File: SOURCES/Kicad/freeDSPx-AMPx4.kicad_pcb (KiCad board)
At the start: 2 copper layers, 60 x 100 mm, 283 parts, among them P1 CONN_01X02, P2 STDCONN, P3 CONN_01X02, P4 CONN_01X02, P5 CONN_01X02, P6 CONN_01X02, U1 LM2841X, U2 TAS5720M, U3 TAS5720M, U4 TAS5720M, U5 TAS5720M

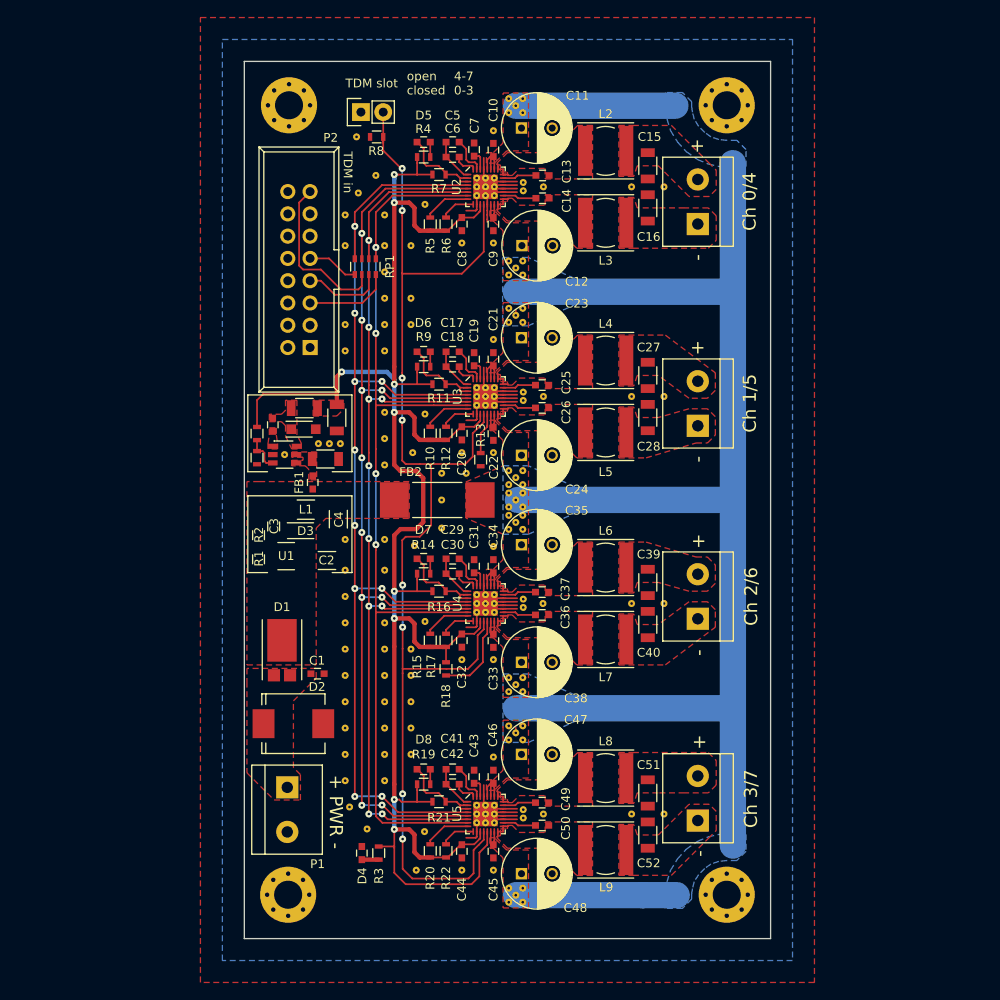
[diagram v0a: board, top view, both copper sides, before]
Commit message: Changed VQFN footprint to solderable.
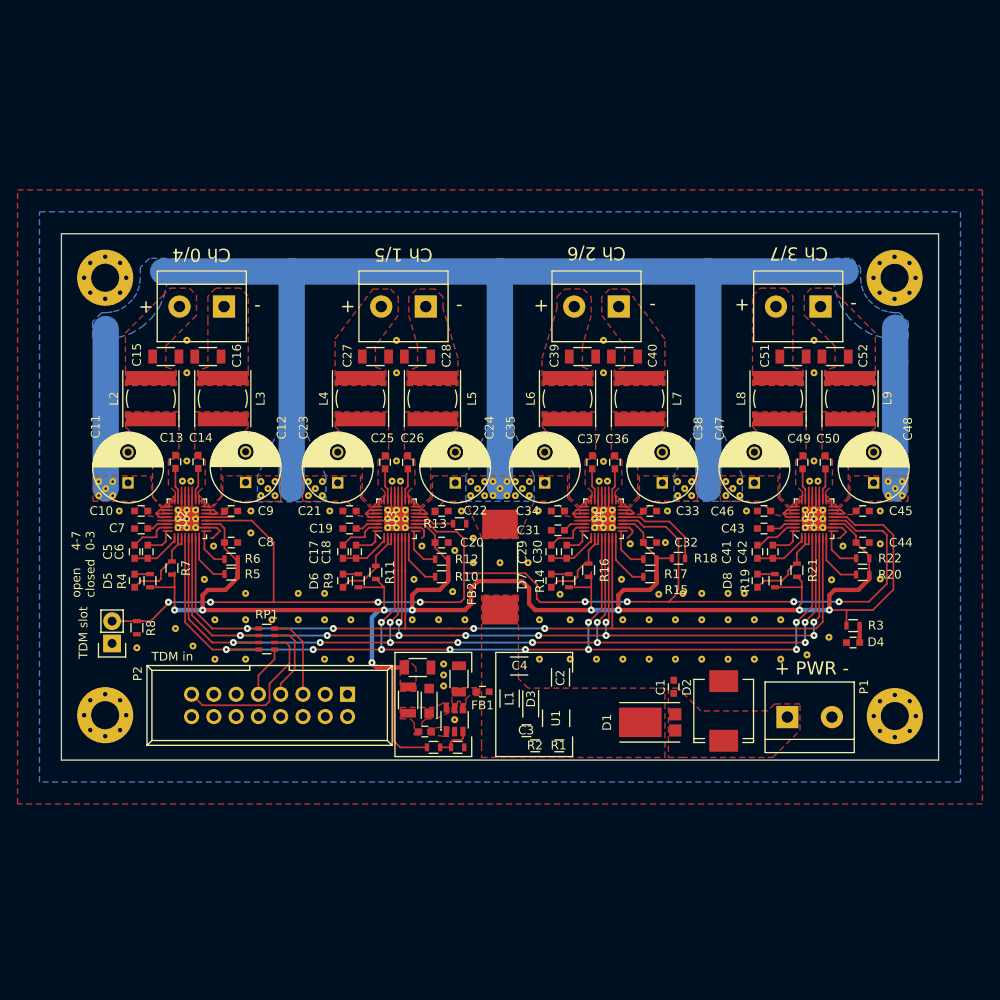
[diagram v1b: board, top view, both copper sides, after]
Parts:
- removed the   at (116.0, 126.5)
- removed the   at (112.5, 135.8)
- removed the   at (112.5, 136.8)
- removed the   at (132.8, 135.8)
- removed the   at (116.8, 145.8)
- removed the   at (116.0, 145.1)
- removed ? (x4): MountingHole_3.2mm_M3_Pad_Via, fdsp_drillhole:MountingHole_3.2mm_M3_Pad_Via
- added  : , fdsp_drillhole:Via_0.3mm_0.8mm, F.Cu at (153.2, 105.2)
- added  : , fdsp_drillhole:Via_0.3mm_0.8mm, F.Cu at (81.5, 105.2)
- added  : , fdsp_drillhole:Via_0.3mm_0.8mm, F.Cu at (105.2, 105.2)
- added  : , fdsp_drillhole:Via_0.3mm_0.8mm, F.Cu at (129.0, 105.0)
- added  : , fdsp_drillhole:Via_0.3mm_0.8mm, F.Cu at (159.2, 98.7)
- added  : , fdsp_drillhole:Via_0.3mm_0.8mm, F.Cu at (160.0, 97.9)
- added  : , fdsp_drillhole:Via_0.3mm_0.8mm, F.Cu at (150.0, 81.8)
- added  : , fdsp_drillhole:Via_0.3mm_0.8mm, F.Cu at (151.0, 102.1)
- added  : , fdsp_drillhole:Via_0.3mm_0.8mm, F.Cu at (150.0, 102.1)
- added  : , fdsp_drillhole:Via_0.3mm_0.8mm, F.Cu at (140.7, 98.7)
- added H1: MountingHole, MountingHole:MountingHole_3.2mm_M3_Pad_Via, F.Cu at (69.1, 74.7)
- added H2: MountingHole, MountingHole:MountingHole_3.2mm_M3_Pad_Via, F.Cu at (159.1, 74.7)
- added H3: MountingHole, MountingHole:MountingHole_3.2mm_M3_Pad_Via, F.Cu at (69.1, 124.5)
- added H4: MountingHole, MountingHole:MountingHole_3.2mm_M3_Pad_Via, F.Cu at (159.2, 124.6)
- U2, U3, U4, U5: footprint fdsp_housing:VQFN-32_4x4mm_Pitch0.4mm -> Library:VQFN-32-handsolder
- moved JP1 66.9 mm to (69.9, 116.3), turned to 180 degrees
- moved   65.1 mm to (68.4, 97.9), turned to 90 degrees
- moved   65.1 mm to (68.4, 99.5), turned to 90 degrees
- moved   64.5 mm to (160.0, 99.5), turned to 90 degrees
- moved   64.0 mm to (69.2, 98.7), turned to 90 degrees
- moved   63.4 mm to (72.8, 116.8), turned to 90 degrees
- moved   62.9 mm to (70.0, 97.9), turned to 90 degrees
- moved   62.8 mm to (70.0, 99.5), turned to 90 degrees
- moved   62.5 mm to (157.5, 109.0), turned to 90 degrees
- moved   62.3 mm to (158.4, 97.9), turned to 90 degrees
- moved R8 62.3 mm to (72.8, 114.6), turned to 90 degrees
- moved   62.2 mm to (158.4, 99.5), turned to 90 degrees
- moved D4 60.9 mm to (154.4, 116.2), turned to 0 degrees
- moved   60.8 mm to (70.8, 101.2), turned to 90 degrees
- moved   60.5 mm to (157.5, 105.0), turned to 90 degrees
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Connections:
- C13 pad 1: Net-(C13-Pad1) -> unconnected-(U2-BST_P-Pad23)
- C14 pad 2: Net-(C14-Pad2) -> unconnected-(U2-BST_N-Pad18)
- C15 pad 2: Net-(C15-Pad2) -> (no net)
- C16 pad 2: Net-(C16-Pad2) -> (no net)
- C17 pad 1: Net-(C17-Pad1) -> unconnected-(U3-VREG-Pad31)
- C17 pad 2: Net-(C17-Pad2) -> unconnected-(U3-VREF_N-Pad1)
- C18 pad 1: Net-(C18-Pad1) -> unconnected-(U3-VCOM-Pad32)
- C18 pad 2: Net-(C17-Pad2) -> unconnected-(U3-VREF_N-Pad1)
- C19 pad 2: Net-(C19-Pad2) -> unconnected-(U3-GVDD-Pad30)
- C25 pad 1: Net-(C25-Pad1) -> unconnected-(U3-BST_P-Pad23)
- C26 pad 2: Net-(C26-Pad2) -> unconnected-(U3-BST_N-Pad18)
- C27 pad 2: Net-(C27-Pad2) -> (no net)
- C28 pad 2: Net-(C28-Pad2) -> (no net)
- C29 pad 1: Net-(C29-Pad1) -> unconnected-(U4-VREG-Pad31)
- C29 pad 2: Net-(C29-Pad2) -> unconnected-(U4-VREF_N-Pad1)
- C30 pad 1: Net-(C30-Pad1) -> unconnected-(U4-VCOM-Pad32)
- C30 pad 2: Net-(C29-Pad2) -> unconnected-(U4-VREF_N-Pad1)
- C31 pad 2: Net-(C31-Pad2) -> unconnected-(U4-GVDD-Pad30)
- C37 pad 1: Net-(C37-Pad1) -> unconnected-(U4-BST_P-Pad23)
- C38 pad 2: Net-(C38-Pad2) -> unconnected-(U4-BST_N-Pad18)
- C39 pad 2: Net-(C39-Pad2) -> (no net)
- C40 pad 2: Net-(C40-Pad2) -> (no net)
- C41 pad 1: Net-(C41-Pad1) -> unconnected-(U5-VREG-Pad31)
- C41 pad 2: Net-(C41-Pad2) -> unconnected-(U5-VREF_N-Pad1)
- C42 pad 1: Net-(C42-Pad1) -> unconnected-(U5-VCOM-Pad32)
- C42 pad 2: Net-(C41-Pad2) -> unconnected-(U5-VREF_N-Pad1)
- C43 pad 2: Net-(C43-Pad2) -> unconnected-(U5-GVDD-Pad30)
- C49 pad 1: Net-(C49-Pad1) -> unconnected-(U5-BST_P-Pad23)
- C5 pad 1: Net-(C5-Pad1) -> unconnected-(U2-VREG-Pad31)
- C5 pad 2: Net-(C5-Pad2) -> unconnected-(U2-VREF_N-Pad1)
- C50 pad 2: Net-(C50-Pad2) -> unconnected-(U5-BST_N-Pad18)
- C51 pad 2: Net-(C51-Pad2) -> (no net)
- C52 pad 2: Net-(C52-Pad2) -> (no net)
- C6 pad 1: Net-(C6-Pad1) -> unconnected-(U2-VCOM-Pad32)
- C6 pad 2: Net-(C5-Pad2) -> unconnected-(U2-VREF_N-Pad1)
- C7 pad 2: Net-(C7-Pad2) -> unconnected-(U2-GVDD-Pad30)
- D5 pad 2: Net-(D5-Pad2) -> (no net)
- D6 pad 2: Net-(D6-Pad2) -> (no net)
- D7 pad 2: Net-(D7-Pad2) -> (no net)
- D8 pad 2: Net-(D8-Pad2) -> (no net)
- L2 pad 2: Net-(C15-Pad2) -> (no net)
- L3 pad 2: Net-(C16-Pad2) -> (no net)
- L4 pad 2: Net-(C27-Pad2) -> (no net)
- L5 pad 2: Net-(C28-Pad2) -> (no net)
- L6 pad 2: Net-(C39-Pad2) -> (no net)
- L7 pad 2: Net-(C40-Pad2) -> (no net)
- L8 pad 2: Net-(C51-Pad2) -> (no net)
- L9 pad 2: Net-(C52-Pad2) -> (no net)
- P2 pad 1: Net-(P2-Pad1) -> unconnected-(P2-V+-Pad1)
- P2 pad 11: Net-(P2-Pad11) -> unconnected-(P2-SDA-Pad11)
- P2 pad 13: Net-(P2-Pad13) -> unconnected-(P2-SCL-Pad13)
- P2 pad 3: Net-(P2-Pad3) -> unconnected-(P2-MDI-Pad3)
- P3 pad 1: Net-(C16-Pad2) -> (no net)
- P3 pad 2: Net-(C15-Pad2) -> (no net)
- P4 pad 1: Net-(C28-Pad2) -> (no net)
- P4 pad 2: Net-(C27-Pad2) -> (no net)
- P5 pad 1: Net-(C40-Pad2) -> (no net)
- P5 pad 2: Net-(C39-Pad2) -> (no net)
- P6 pad 1: Net-(C52-Pad2) -> (no net)
- P6 pad 2: Net-(C51-Pad2) -> (no net)
- R10 pad 2: Net-(R10-Pad2) -> unconnected-(U3-SCL-Pad8)
- R12 pad 2: Net-(R12-Pad2) -> unconnected-(U3-SDA-Pad9)
- R13 pad 2: Net-(R13-Pad2) -> unconnected-(U3-ADR0-Pad13)
- R14 pad 2: Net-(D7-Pad2) -> (no net)
- R15 pad 2: Net-(R15-Pad2) -> unconnected-(U4-SCL-Pad8)
- R17 pad 2: Net-(R17-Pad2) -> unconnected-(U4-SDA-Pad9)
- R18 pad 1: Net-(R18-Pad1) -> unconnected-(U4-ADR0-Pad13)
- R19 pad 2: Net-(D8-Pad2) -> (no net)
- R20 pad 2: Net-(R20-Pad2) -> unconnected-(U5-SCL-Pad8)
- R22 pad 2: Net-(R22-Pad2) -> unconnected-(U5-SDA-Pad9)
- R4 pad 2: Net-(D5-Pad2) -> (no net)
- R5 pad 2: Net-(R5-Pad2) -> unconnected-(U2-SCL-Pad8)
- R6 pad 2: Net-(R6-Pad2) -> unconnected-(U2-SDA-Pad9)
- R9 pad 2: Net-(D6-Pad2) -> (no net)
- U2 pad 1: Net-(C5-Pad2) -> unconnected-(U2-VREF_N-Pad1)
- U2 pad 18: Net-(C14-Pad2) -> unconnected-(U2-BST_N-Pad18)
- U2 pad 23: Net-(C13-Pad1) -> unconnected-(U2-BST_P-Pad23)
- U2 pad 30: Net-(C7-Pad2) -> unconnected-(U2-GVDD-Pad30)
- U2 pad 31: Net-(C5-Pad1) -> unconnected-(U2-VREG-Pad31)
- U2 pad 32: Net-(C6-Pad1) -> unconnected-(U2-VCOM-Pad32)
- U2 pad 8: Net-(R5-Pad2) -> unconnected-(U2-SCL-Pad8)
- U2 pad 9: Net-(R6-Pad2) -> unconnected-(U2-SDA-Pad9)
- U3 pad 1: Net-(C17-Pad2) -> unconnected-(U3-VREF_N-Pad1)
- U3 pad 13: Net-(R13-Pad2) -> unconnected-(U3-ADR0-Pad13)
- U3 pad 18: Net-(C26-Pad2) -> unconnected-(U3-BST_N-Pad18)
- U3 pad 23: Net-(C25-Pad1) -> unconnected-(U3-BST_P-Pad23)
- U3 pad 30: Net-(C19-Pad2) -> unconnected-(U3-GVDD-Pad30)
- U3 pad 31: Net-(C17-Pad1) -> unconnected-(U3-VREG-Pad31)
- U3 pad 32: Net-(C18-Pad1) -> unconnected-(U3-VCOM-Pad32)
- U3 pad 8: Net-(R10-Pad2) -> unconnected-(U3-SCL-Pad8)
- U3 pad 9: Net-(R12-Pad2) -> unconnected-(U3-SDA-Pad9)
- U4 pad 1: Net-(C29-Pad2) -> unconnected-(U4-VREF_N-Pad1)
- U4 pad 13: Net-(R18-Pad1) -> unconnected-(U4-ADR0-Pad13)
- U4 pad 18: Net-(C38-Pad2) -> unconnected-(U4-BST_N-Pad18)
- U4 pad 23: Net-(C37-Pad1) -> unconnected-(U4-BST_P-Pad23)
- U4 pad 30: Net-(C31-Pad2) -> unconnected-(U4-GVDD-Pad30)
- U4 pad 31: Net-(C29-Pad1) -> unconnected-(U4-VREG-Pad31)
- U4 pad 32: Net-(C30-Pad1) -> unconnected-(U4-VCOM-Pad32)
- U4 pad 8: Net-(R15-Pad2) -> unconnected-(U4-SCL-Pad8)
- U4 pad 9: Net-(R17-Pad2) -> unconnected-(U4-SDA-Pad9)
- U5 pad 1: Net-(C41-Pad2) -> unconnected-(U5-VREF_N-Pad1)
- U5 pad 18: Net-(C50-Pad2) -> unconnected-(U5-BST_N-Pad18)
- U5 pad 23: Net-(C49-Pad1) -> unconnected-(U5-BST_P-Pad23)
- U5 pad 30: Net-(C43-Pad2) -> unconnected-(U5-GVDD-Pad30)
- U5 pad 31: Net-(C41-Pad1) -> unconnected-(U5-VREG-Pad31)
- U5 pad 32: Net-(C42-Pad1) -> unconnected-(U5-VCOM-Pad32)
- U5 pad 8: Net-(R20-Pad2) -> unconnected-(U5-SCL-Pad8)
- U5 pad 9: Net-(R22-Pad2) -> unconnected-(U5-SDA-Pad9)
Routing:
- net (no net): track 45.0 -> 7.50 mm
- net unconnected-(U4-ADR0-Pad13): track 0.00 -> 10.7 mm
- net +3V3: track 208.9 -> 219.5 mm
- net Net-(R18-Pad1): track 9.73 -> 0.00 mm
- net unconnected-(U5-SCL-Pad8): track 0.00 -> 6.78 mm
- net unconnected-(U4-SCL-Pad8): track 0.00 -> 6.64 mm
- net unconnected-(U3-SCL-Pad8): track 0.00 -> 6.49 mm
- net unconnected-(U5-VREF_N-Pad1): track 0.00 -> 6.37 mm
- net unconnected-(U2-SCL-Pad8): track 0.00 -> 6.23 mm
- net unconnected-(U3-VREF_N-Pad1): track 0.00 -> 6.02 mm
- net unconnected-(U4-VREF_N-Pad1): track 0.00 -> 5.87 mm
- net unconnected-(U2-VREF_N-Pad1): track 0.00 -> 5.87 mm
- net Net-(R5-Pad2): track 5.43 -> 0.00 mm
- net Net-(R10-Pad2): track 5.41 -> 0.00 mm
- net Net-(R20-Pad2): track 5.41 -> 0.00 mm
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- added copper zone on F.Cu, net (none)
- removed copper zone on F.Cu, net Net-(C15-Pad2)
- removed copper zone on F.Cu, net Net-(C16-Pad2)
- removed copper zone on F.Cu, net Net-(C27-Pad2)
- removed copper zone on F.Cu, net Net-(C28-Pad2)
- removed copper zone on F.Cu, net Net-(C39-Pad2)
- removed copper zone on F.Cu, net Net-(C40-Pad2)
- removed copper zone on F.Cu, net Net-(C51-Pad2)
- removed copper zone on F.Cu, net Net-(C52-Pad2)
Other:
- board size 60 x 100 mm -> 100 x 60 mm
- net class 3V3 removed
- net class Default removed
- net class VCC removed

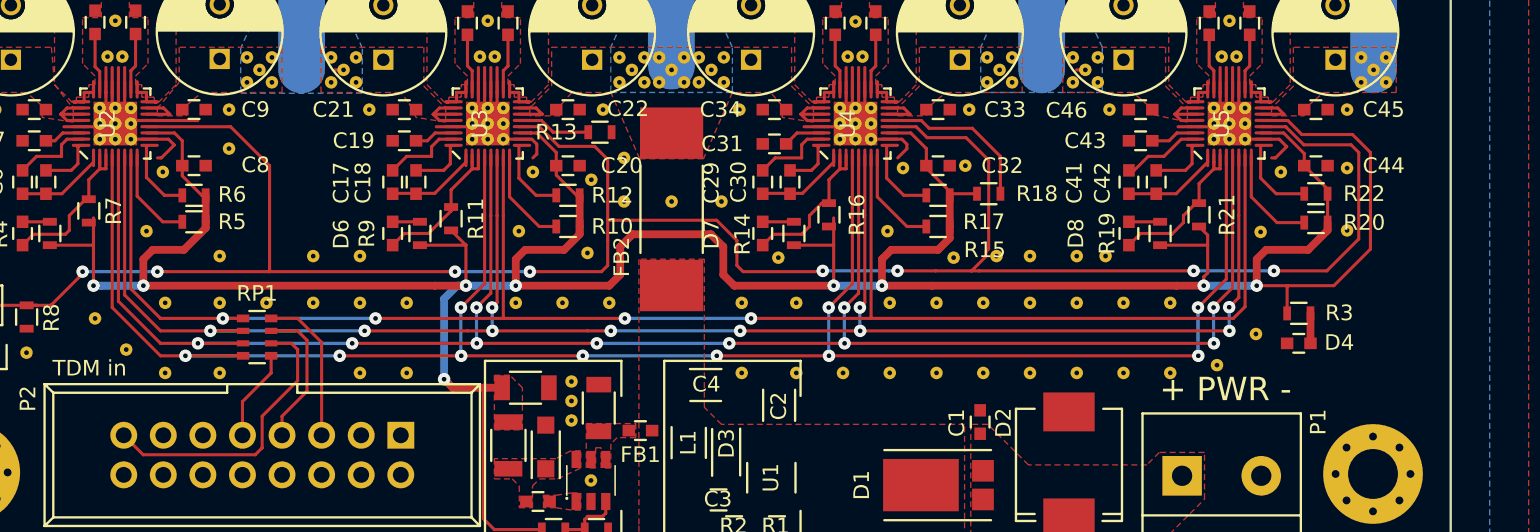
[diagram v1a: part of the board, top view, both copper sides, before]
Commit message: Changed heat disipation Vias to a big one to solder through.
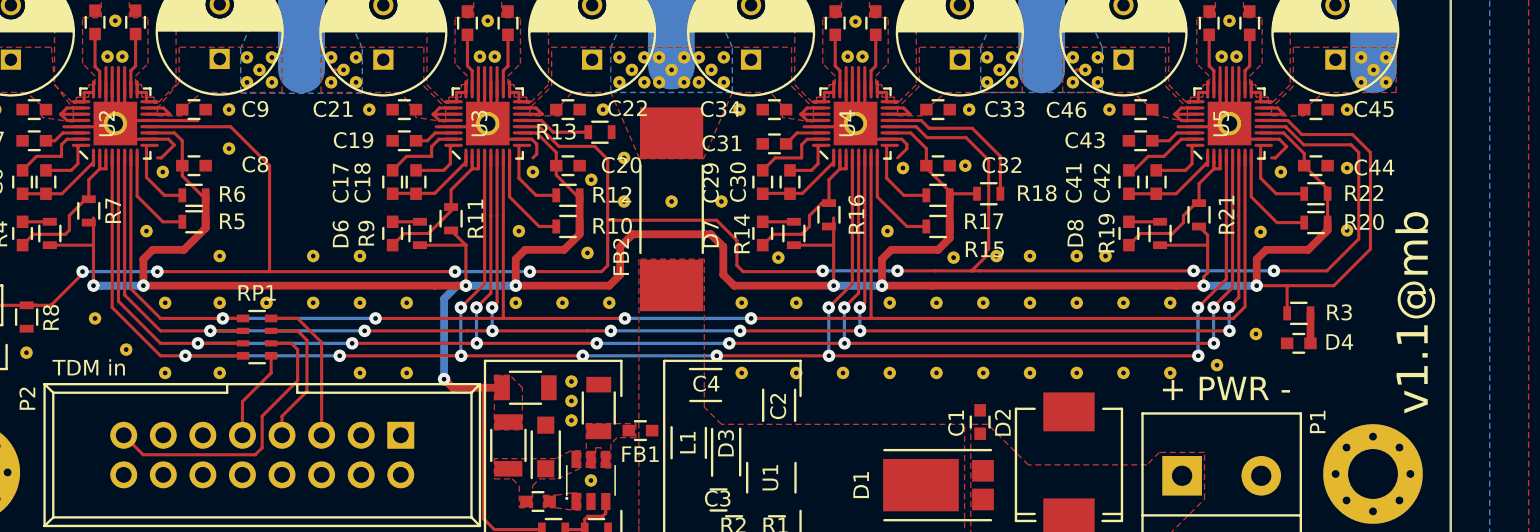
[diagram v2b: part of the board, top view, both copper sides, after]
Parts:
- removed the   at (77.5, 103.1)
- removed the   at (78.5, 103.1)
- removed the   at (79.5, 103.1)
- removed the   at (151.0, 102.1)
- removed the   at (151.0, 103.1)
- removed the   at (150.0, 101.1)
- removed the   at (151.0, 101.1)
- removed the   at (79.5, 102.1)
- removed the   at (149.0, 102.1)
- removed the   at (149.0, 103.1)
- removed the   at (150.0, 103.1)
- removed the   at (149.0, 101.1)
- removed the   at (77.5, 102.1)
- removed the   at (102.4, 101.1)
- removed the   at (102.4, 103.1)
- removed the   at (101.4, 103.1)
- removed the   at (103.4, 103.1)
- removed the   at (103.4, 101.1)
- removed the   at (103.4, 102.1)
- removed the   at (101.4, 101.1)
- removed the   at (101.4, 102.1)
- removed the   at (79.5, 101.1)
- removed the   at (77.5, 101.1)
- removed the   at (125.0, 101.1)
- removed the   at (78.5, 101.1)
- removed the   at (127.0, 101.1)
- removed the   at (125.0, 103.1)
- removed the   at (125.0, 102.1)
- removed the   at (126.0, 101.1)
- removed the   at (126.0, 103.1)
- removed the   at (127.0, 103.1)
- removed the   at (127.0, 102.1)
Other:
- board text added: "v1.1@mb"
